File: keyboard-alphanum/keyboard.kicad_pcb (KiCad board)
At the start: 2 copper layers, 76.2 x 100.8 mm, 52 parts, among them J1 USB_B_Mini, U1 ATmega168PA-A, U2 CH340C, Y1 16MHz

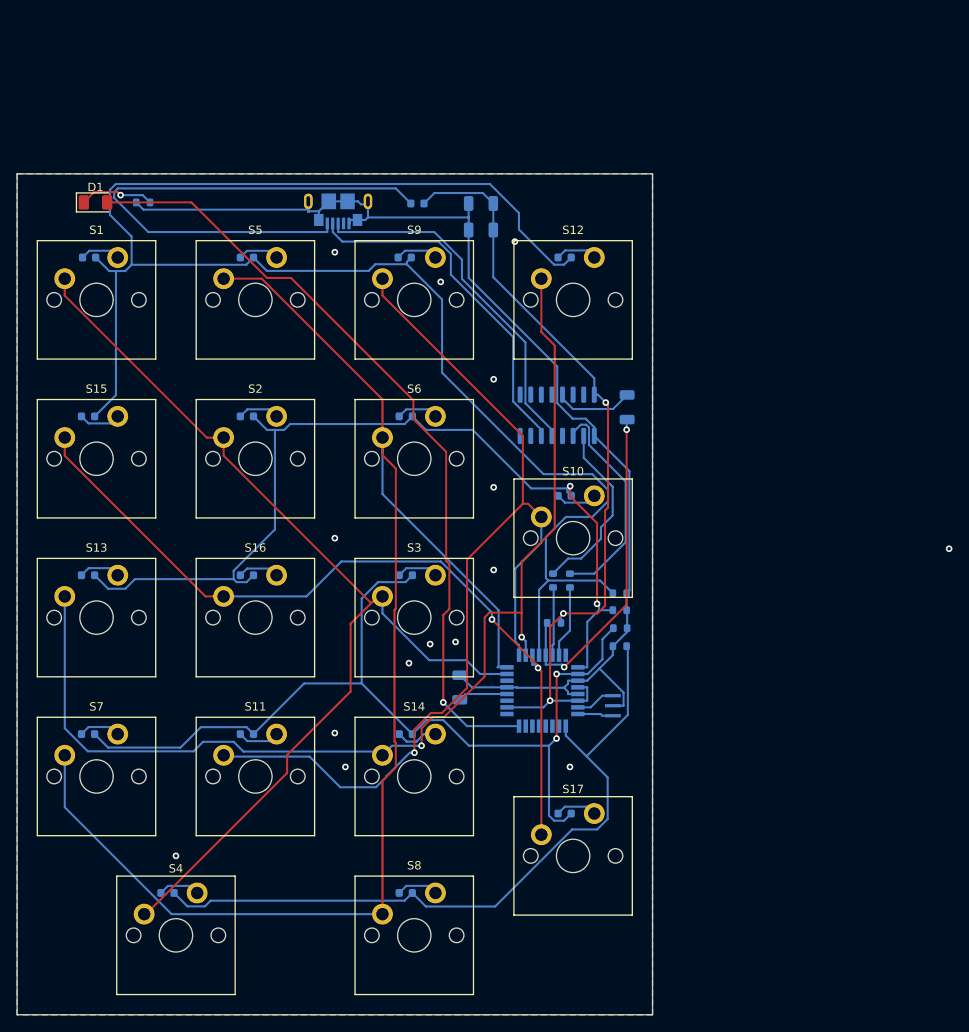
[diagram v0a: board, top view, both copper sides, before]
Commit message: Update keyboar pcb design
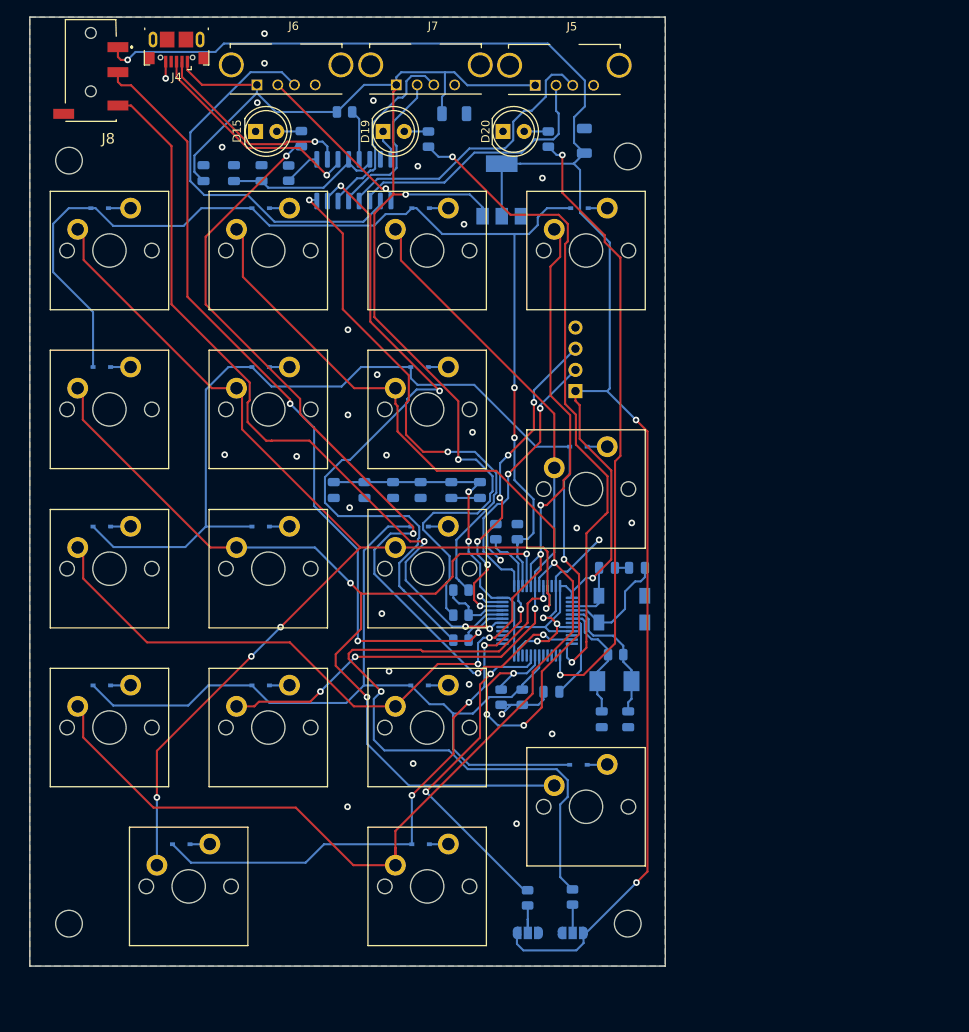
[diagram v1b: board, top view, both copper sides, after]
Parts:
- removed S1: NL, Switch_Keyboard_Cherry_MX:SW_Cherry_MX_PCB_1.00u
- removed S10: plus, Switch_Keyboard_Cherry_MX:SW_Cherry_MX_PCB_2.00u_90deg
- removed S11: 2, Switch_Keyboard_Cherry_MX:SW_Cherry_MX_PCB_1.00u
- removed S12: sub, Switch_Keyboard_Cherry_MX:SW_Cherry_MX_PCB_1.00u
- removed S13: 4, Switch_Keyboard_Cherry_MX:SW_Cherry_MX_PCB_1.00u
- removed S14: 3, Switch_Keyboard_Cherry_MX:SW_Cherry_MX_PCB_1.00u
- removed S15: 7, Switch_Keyboard_Cherry_MX:SW_Cherry_MX_PCB_1.00u
- removed S16: 5, Switch_Keyboard_Cherry_MX:SW_Cherry_MX_PCB_1.00u
- removed S17: enter, Switch_Keyboard_Cherry_MX:SW_Cherry_MX_PCB_2.00u_90deg
- removed S2: 8, Switch_Keyboard_Cherry_MX:SW_Cherry_MX_PCB_1.00u
- removed S3: 6, Switch_Keyboard_Cherry_MX:SW_Cherry_MX_PCB_1.00u
- removed S4: 0, Switch_Keyboard_Cherry_MX:SW_Cherry_MX_PCB_2.00u
- removed S5: div, Switch_Keyboard_Cherry_MX:SW_Cherry_MX_PCB_1.00u
- removed S6: 9, Switch_Keyboard_Cherry_MX:SW_Cherry_MX_PCB_1.00u
- removed S7: 1, Switch_Keyboard_Cherry_MX:SW_Cherry_MX_PCB_1.00u
- removed S8: point, Switch_Keyboard_Cherry_MX:SW_Cherry_MX_PCB_1.00u
- removed S9: mul, Switch_Keyboard_Cherry_MX:SW_Cherry_MX_PCB_1.00u
- added C10: 10nF, Capacitor_SMD:C_0805_2012Metric, B.Cu at (154.4, 91.0)
- added C11: 1uF, Capacitor_SMD:C_0805_2012Metric, B.Cu at (150.7, 91.0)
- added C12: 22uF, Capacitor_SMD:C_1206_3216Metric, B.Cu at (180.8, 49.1)
- added C13: 10uF, Capacitor_SMD:C_1206_3216Metric, B.Cu at (165.2, 45.9)
- added C14: 4.7uF, Capacitor_SMD:C_0805_2012Metric, B.Cu at (142.1, 53.0)
- added C15: 100nF, Capacitor_SMD:C_0805_2012Metric, B.Cu at (138.8, 53.0)
- added C16: 4.7uF, Capacitor_SMD:C_0805_2012Metric, B.Cu at (135.1, 53.0)
- added C5: 100nF, Capacitor_SMD:C_0805_2012Metric, B.Cu at (176.8, 115.2)
- added C6: 100nF, Capacitor_SMD:C_0805_2012Metric, B.Cu at (168.3, 91.0)
- added C7: 100nF, Capacitor_SMD:C_0805_2012Metric, B.Cu at (164.8, 91.0)
- added C8: 100nF, Capacitor_SMD:C_0805_2012Metric, B.Cu at (161.2, 91.0)
- added C9: 4.7uF, Capacitor_SMD:C_0805_2012Metric, B.Cu at (157.9, 91.0)
- added D20: ScrollLock, LED_THT:LED_D5.0mm, F.Cu at (171.0, 48.0)
- added H1: MountingHole_3.2mm_M3, MountingHole:MountingHole_3.2mm_M3, F.Cu at (119.0, 51.5)
- added H2: MountingHole_3.2mm_M3, MountingHole:MountingHole_3.2mm_M3, F.Cu at (186.0, 51.0)
- added H3: MountingHole_3.2mm_M3, MountingHole:MountingHole_3.2mm_M3, F.Cu at (119.0, 143.0)
- added H4: MountingHole_3.2mm_M3, MountingHole:MountingHole_3.2mm_M3, F.Cu at (186.0, 143.0)
- added J2: BOOT1, Jumper:SolderJumper-3_P1.3mm_Open_RoundedPad1.0x1.5mm, B.Cu at (174.0, 144.1)
- added J3: ST-Link, Connector_PinHeader_2.54mm:PinHeader_1x04_P2.54mm_Vertical, B.Cu at (179.7, 79.1)
- added J4: USB_B_Mini, common:USB_Micro-B_A01SB141B1-245, F.Cu at (131.9, 38.2)
- added J5: USB_A, common:USB_A_Molex_105057_Vertical, F.Cu at (174.9, 42.5)
- added J6: USB_A, common:USB_A_Molex_105057_Vertical, F.Cu at (141.5, 42.4)
- added J7: USB_A, common:USB_A_Molex_105057_Vertical, F.Cu at (158.2, 42.4)
- added J8: UART, common:PJ320D, F.Cu at (121.6, 40.7)
- added R10: 1K, Resistor_SMD:R_0805_2012Metric, B.Cu at (170.2, 96.0)
- added R11: 100K, Resistor_SMD:R_0805_2012Metric, B.Cu at (145.3, 53.0)
- added R12: 4.7K, Resistor_SMD:R_0805_2012Metric, B.Cu at (152.0, 45.7)
- added R13: 100K, Resistor_SMD:R_0805_2012Metric, B.Cu at (176.5, 48.9)
- added R14: 100K, Resistor_SMD:R_0805_2012Metric, B.Cu at (162.1, 48.9)
- added R15: 100K, Resistor_SMD:R_0805_2012Metric, B.Cu at (146.9, 48.9)
- added R9: 1K, Resistor_SMD:R_0805_2012Metric, B.Cu at (173.4, 115.8)
- added SW1: NL, Switch_Keyboard_Cherry_MX:SW_Cherry_MX_PCB_1.00u, F.Cu at (123.9, 62.3)
- added SW10: plus, Switch_Keyboard_Cherry_MX:SW_Cherry_MX_PCB_2.00u_90deg, F.Cu at (181.0, 90.9)
- added SW11: 2, Switch_Keyboard_Cherry_MX:SW_Cherry_MX_PCB_1.00u, F.Cu at (142.9, 119.5)
- added SW12: sub, Switch_Keyboard_Cherry_MX:SW_Cherry_MX_PCB_1.00u, F.Cu at (181.0, 62.3)
- added SW13: 4, Switch_Keyboard_Cherry_MX:SW_Cherry_MX_PCB_1.00u, F.Cu at (123.9, 100.4)
- added SW14: 3, Switch_Keyboard_Cherry_MX:SW_Cherry_MX_PCB_1.00u, F.Cu at (162.0, 119.5)
- added SW15: 7, Switch_Keyboard_Cherry_MX:SW_Cherry_MX_PCB_1.00u, F.Cu at (123.9, 81.3)
- added SW16: 5, Switch_Keyboard_Cherry_MX:SW_Cherry_MX_PCB_1.00u, F.Cu at (142.9, 100.4)
- added SW17: enter, Switch_Keyboard_Cherry_MX:SW_Cherry_MX_PCB_2.00u_90deg, F.Cu at (181.0, 129.0)
- added SW2: 8, Switch_Keyboard_Cherry_MX:SW_Cherry_MX_PCB_1.00u, F.Cu at (142.9, 81.3)
- added SW3: 6, Switch_Keyboard_Cherry_MX:SW_Cherry_MX_PCB_1.00u, F.Cu at (162.0, 100.4)
- added SW4: 0, Switch_Keyboard_Cherry_MX:SW_Cherry_MX_PCB_2.00u, F.Cu at (133.3, 138.5)
- added SW5: div, Switch_Keyboard_Cherry_MX:SW_Cherry_MX_PCB_1.00u, F.Cu at (142.9, 62.3)
- added SW6: 9, Switch_Keyboard_Cherry_MX:SW_Cherry_MX_PCB_1.00u, F.Cu at (162.0, 81.3)
- added SW7: 1, Switch_Keyboard_Cherry_MX:SW_Cherry_MX_PCB_1.00u, F.Cu at (123.9, 119.5)
- added SW8: dot, Switch_Keyboard_Cherry_MX:SW_Cherry_MX_PCB_1.00u, F.Cu at (162.0, 138.5)
- added SW9: mul, Switch_Keyboard_Cherry_MX:SW_Cherry_MX_PCB_1.00u, F.Cu at (162.0, 62.3)
- added U3: HS8836A, Package_SO:SOP-16_3.9x9.9mm_P1.27mm, B.Cu at (153.2, 53.8)
- added Y2: 32768MHz, Crystal:Crystal_SMD_SeikoEpson_MC306-4Pin_8.0x3.2mm, B.Cu at (185.3, 105.3)
- C1, C2, C4: value 0.1uF -> 22pF; footprint common:C_1206_3216Metric -> Capacitor_SMD:C_0805_2012Metric
- C3: value 10uF -> 22pF; footprint common:C_1206_3216Metric -> Capacitor_SMD:C_0805_2012Metric
- D1: value LED -> D_Small; footprint common:LED_1206_3216Metric -> Diode_SMD:D_SOD-323; moved to B.Cu
- D10, D11, D12, D13, D14, D16, D17, D18, D2, D3, D4, D5, D6, D7, D8, D9: value D -> D_Small; footprint common:D_0603_1608Metric -> Diode_SMD:D_SOD-323
- D15: value D -> NumLock; footprint common:D_0603_1608Metric -> LED_THT:LED_D5.0mm; moved to F.Cu
- D19: value D -> CapsLock; footprint common:D_0603_1608Metric -> LED_THT:LED_D5.0mm; moved to F.Cu
- J1: value USB_B_Mini -> BOOT0; footprint common:USB_Micro-B_GCT_USB3076-30-A -> Jumper:SolderJumper-3_P1.3mm_Open_RoundedPad1.0x1.5mm
- R1, R2: value 1K -> 100K; footprint common:R_0603_1608Metric -> Resistor_SMD:R_0805_2012Metric
- R3: value 1K -> 1M; footprint common:R_0603_1608Metric -> Resistor_SMD:R_0805_2012Metric
- R4: value 1K -> 4.7K; footprint common:R_0603_1608Metric -> Resistor_SMD:R_0805_2012Metric
- R5, R6: value 1K -> 20R; footprint common:R_0603_1608Metric -> Resistor_SMD:R_0805_2012Metric
- R7, R8: footprint common:R_0603_1608Metric -> Resistor_SMD:R_0805_2012Metric
- U1: value ATmega168PA-A -> STM32F103C6T6A; footprint Package_QFP:TQFP-32_7x7mm_P0.8mm -> Package_QFP:LQFP-48_7x7mm_P0.5mm
- U2: value CH340C -> LD1117S33TR; footprint Package_SO:SOIC-16_3.9x9.9mm_P1.27mm -> Package_TO_SOT_SMD:SOT-223-3_TabPin2
- Y1: value 16MHz -> 8MHz; footprint common:Resonator_SMD_Murata_CSTxExxV-3Pin_3.0x1.1mm -> Crystal:Crystal_SMD_Abracon_ABM3-2Pin_5.0x3.2mm
- moved R2 95.3 mm to (174.0, 139.9), turned to 90 degrees
- moved J1 91.0 mm to (179.4, 144.1), turned to 180 degrees
- moved D19 84.6 mm to (156.7, 48.0), turned to 0 degrees
- moved D5 82.9 mm to (142.0, 57.2), turned to 0 degrees
- moved D9 74.6 mm to (161.2, 57.2), turned to 0 degrees
- moved C2 64.3 mm to (186.1, 118.5), turned to 90 degrees
- moved D10 57.4 mm to (180.1, 85.8), turned to 0 degrees
- moved D16 57.2 mm to (122.9, 76.3), turned to 0 degrees
- moved D15 56.9 mm to (141.4, 48.0), turned to 0 degrees
- moved D14 54.2 mm to (161.0, 114.4), turned to 0 degrees
- moved D7 54.2 mm to (122.9, 114.4), turned to 0 degrees
- moved D11 54.1 mm to (142.0, 114.4), turned to 0 degrees
- moved D8 51.3 mm to (161.2, 133.5), turned to 0 degrees
- moved D18 45.8 mm to (180.1, 124.0), turned to 0 degrees
- moved C3 44.6 mm to (187.1, 100.3), turned to 0 degrees
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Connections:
- C1 pad 2: Net-(C1-Pad2) -> OSC_OUT
- C2 pad 1: +5V -> GND
- C2 pad 2: GND -> OSC_IN
- C3 pad 1: +5V -> GND
- C3 pad 2: GND -> OSC32_OUT
- C4 pad 1: Net-(C4-Pad1) -> GND
- C4 pad 2: RESET -> OSC32_IN
- D1 pad 1: Net-(D1-Pad1) -> I0
- D10 pad 1: I3 -> I1
- D11 pad 1: I0 -> I2
- D12 pad 1: I1 -> I0
- D13 pad 1: I2 -> I1
- D14 pad 1: I0 -> I2
- D15 pad 1: I1 -> GND
- D16 pad 1: I2 -> I0
- D17 pad 1: I0 -> I1
- D18 pad 1: I1 -> I2
- D19 pad 1: I2 -> GND
- D2 pad 1: I0 -> I1
- D3 pad 1: I1 -> I2
- D4 pad 1: I2 -> I3
- D5 pad 1: I3 -> I0
- D6 pad 1: +5V -> I1
- D7 pad 1: I0 -> I2
- D8 pad 1: I1 -> I3
- D9 pad 1: I2 -> I0
- J1 pad 1: Net-(D6-Pad2) -> +3.3V
- J1 pad 3: Net-(J1-Pad3) -> GND
- R1 pad 1: RESET -> Net-(J1-Pad2)
- R1 pad 2: +5V -> BOOT0
- R2 pad 1: Net-(D1-Pad1) -> Net-(J2-Pad2)
- R2 pad 2: GND -> BOOT1
- R3 pad 1: Net-(R3-Pad1) -> OSC_IN
- R3 pad 2: RX -> OSC_OUT
- R4 pad 1: Net-(R4-Pad1) -> K-DP
- R4 pad 2: TX -> VBUS
- R5 pad 1: I0 -> Net-(R5-Pad1)
- R5 pad 2: GND -> K-DP
- R6 pad 1: I1 -> Net-(R6-Pad1)
- R6 pad 2: GND -> K-DM
- R7 pad 1: I2 -> I0
- R8 pad 1: I3 -> I1
- U1 pad 1: I1 -> +3.3V
- U1 pad 11: unconnected-(U1-Pad11) -> NumLock
- U1 pad 12: unconnected-(U1-Pad12) -> CapsLock
- U1 pad 13: unconnected-(U1-Pad13) -> ScrLock
- U1 pad 16: Net-(D1-Pad2) -> unconnected-(U1-Pad16)
- U1 pad 18: +5V -> I2
- U1 pad 19: unconnected-(U1-Pad19) -> I1
- U1 pad 2: I2 -> unconnected-(U1-Pad2)
- U1 pad 20: Net-(C1-Pad2) -> BOOT1
- U1 pad 21: GND -> unconnected-(U1-Pad21)
- U1 pad 23: O0 -> GND
- U1 pad 24: O1 -> +3.3V
- U1 pad 25: O2 -> unconnected-(U1-Pad25)
- U1 pad 26: O3 -> unconnected-(U1-Pad26)
- U1 pad 27: O4 -> unconnected-(U1-Pad27)
- U1 pad 28: I0 -> unconnected-(U1-Pad28)
- U1 pad 29: RESET -> unconnected-(U1-Pad29)
- U1 pad 3: GND -> OSC32_IN
- U1 pad 30: RX -> TX
- U1 pad 31: TX -> RX
- U1 pad 32: unconnected-(U1-Pad32) -> K-DM
- U1 pad 4: +5V -> OSC32_OUT
- U1 pad 5: GND -> OSC_IN
- U1 pad 6: +5V -> OSC_OUT
- U1 pad 7: Net-(U1-Pad7) -> NRST
- U1 pad 8: Net-(U1-Pad8) -> GND
- U1 pad 9: I3 -> +3.3V
- U2 pad 2: Net-(R3-Pad1) -> +3.3V
- U2 pad 3: Net-(R4-Pad1) -> VBUS
- Y1 pad 1: Net-(U1-Pad8) -> OSC_IN
- Y1 pad 2: GND -> OSC_OUT
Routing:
- net +3.3V: track 0.00 -> 288.3 mm, vias 0 -> 6
- net VBUS: track 0.00 -> 160.5 mm, vias 0 -> 2
- net NumLock: track 0.00 -> 101.0 mm, vias 0 -> 4
- net +5V: track 94.1 -> 0.00 mm, vias 3 -> 0
- net Net-(D1-Pad2): track 95.1 -> 2.66 mm, vias 1 -> 0
- net RX: track 8.23 -> 99.5 mm, vias 0 -> 3
- net GND: track 141.7 -> 51.8 mm, vias 14 -> 33
- net TX: track 8.67 -> 92.8 mm, vias 0 -> 3
- net Net-(R6-Pad1): track 0.00 -> 83.4 mm, vias 0 -> 2
- net BOOT0: track 0.00 -> 80.8 mm, vias 0 -> 2
- net CapsLock: track 0.00 -> 80.2 mm, vias 0 -> 2
- net ScrLock: track 0.00 -> 74.3 mm, vias 0 -> 2
- net I0: track 204.5 -> 134.2 mm, vias 0 -> 2
- net Net-(R5-Pad1): track 0.00 -> 63.5 mm, vias 0 -> 2
- net Net-(D6-Pad2): track 65.5 -> 2.40 mm
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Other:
- board size 76.2 x 100.8 mm -> 76.2 x 113.8 mm

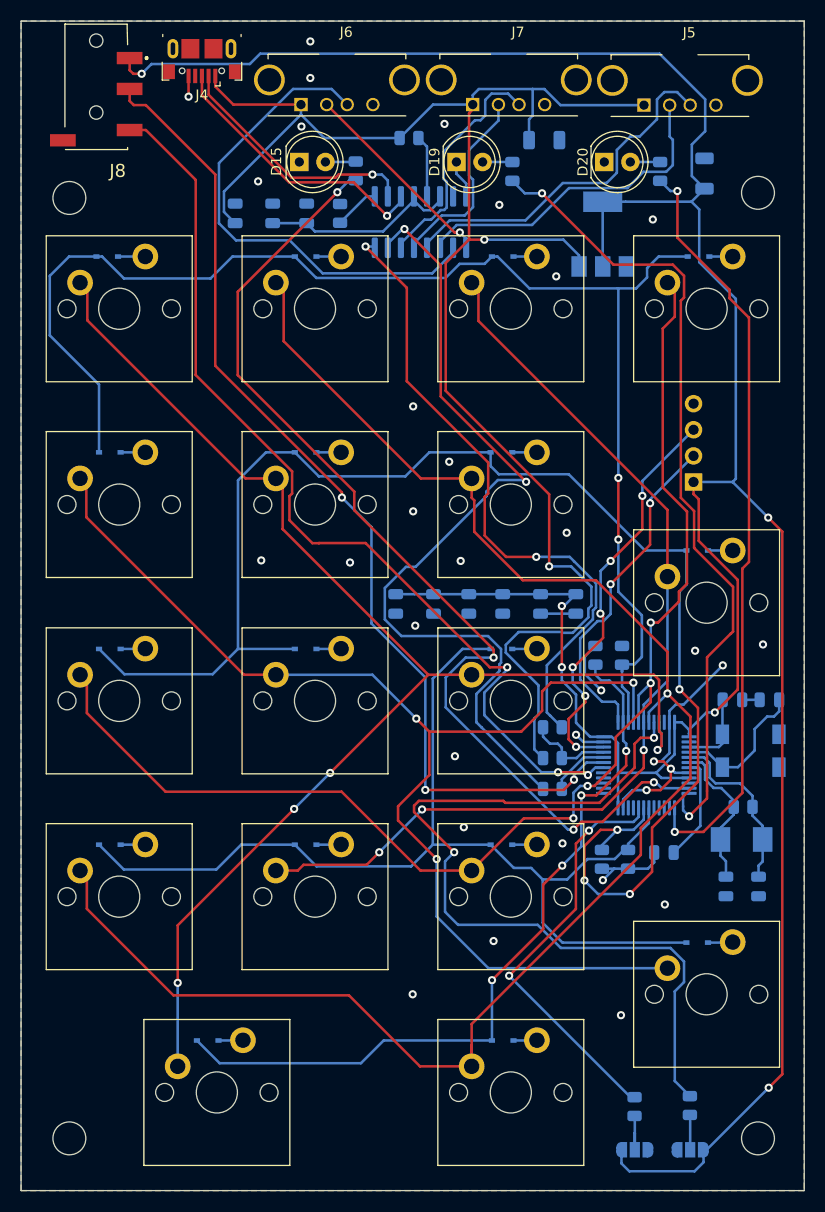
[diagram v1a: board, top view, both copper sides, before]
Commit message: Fix issues and update alphanum keyboard
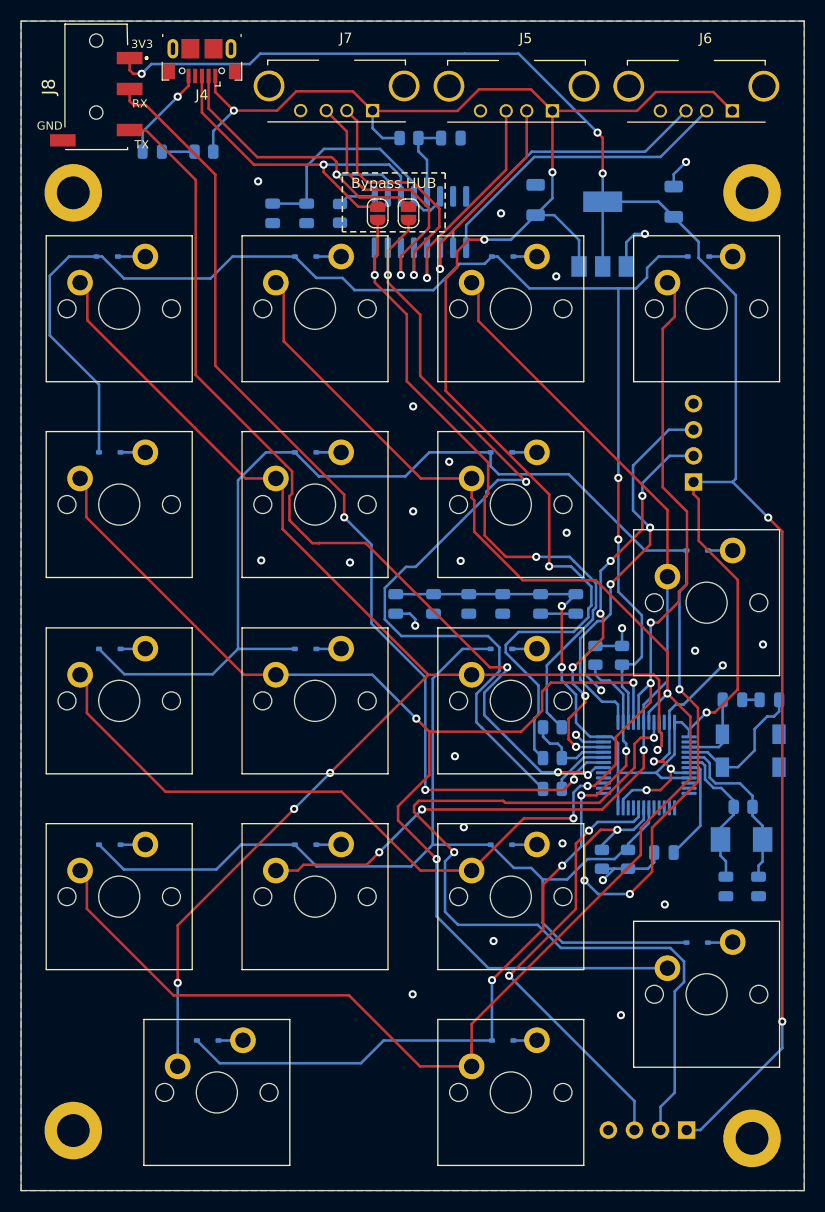
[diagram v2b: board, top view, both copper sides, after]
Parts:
- removed D19: CapsLock, LED_THT:LED_D5.0mm
- removed D20: ScrollLock, LED_THT:LED_D5.0mm
- removed J2: BOOT1, Jumper:SolderJumper-3_P1.3mm_Open_RoundedPad1.0x1.5mm
- removed R13, R14, R15, R2: 100K, Resistor_SMD:R_0805_2012Metric
- removed Y2: 32768MHz, Crystal:Crystal_SMD_SeikoEpson_MC306-4Pin_8.0x3.2mm
- added JP1: SolderJumper_2_Open, Jumper:SolderJumper-2_P1.3mm_Open_RoundedPad1.0x1.5mm, F.Cu at (149.0, 53.0)
- added JP2: SolderJumper_2_Open, Jumper:SolderJumper-2_P1.3mm_Open_RoundedPad1.0x1.5mm, F.Cu at (152.0, 53.0)
- added Y3: 32768MHz, Crystal:Crystal_SMD_SeikoEpson_MC306-4Pin_8.0x3.2mm, B.Cu at (185.3, 105.3)
- D15: value NumLock -> LED; footprint LED_THT:LED_D5.0mm -> LED_SMD:LED_0805_2012Metric; moved to B.Cu
- H1, H2, H3, H4: value MountingHole_3.2mm_M3 -> MountingHole; footprint MountingHole:MountingHole_3.2mm_M3 -> MountingHole:MountingHole_3.2mm_M3_DIN965_Pad
- J1: value BOOT0 -> Prog pings; footprint Jumper:SolderJumper-3_P1.3mm_Open_RoundedPad1.0x1.5mm -> Connector_PinHeader_2.54mm:PinHeader_1x04_P2.54mm_Vertical
- R1: value 100K -> 1K
- R12: value 4.7K -> 4R7
- moved H2 113.0 mm to (119.4, 142.2)
- moved R1 104.2 mm to (132.1, 47.0), turned to 0 degrees
- moved H4 92.0 mm to (185.4, 51.0)
- moved H3 66.4 mm to (185.4, 143.0)
- moved J6 35.0 mm to (176.5, 43.0)
- moved C16 22.2 mm to (156.1, 45.7), turned to 180 degrees
- moved J7 16.8 mm to (141.5, 43.0)
- moved J5 15.9 mm to (159.0, 43.0)
- moved D15 14.3 mm to (127.1, 47.0)
- moved C13 5.89 mm to (164.4, 51.7), turned to 90 degrees
- moved C12 4.06 mm to (177.8, 51.9)
- moved J1 1.95 mm to (179.1, 142.2), turned to 90 degrees
- moved H1 0.63 mm to (119.4, 51.0)
- turned C14 to -90 degrees
- turned C15 to -90 degrees
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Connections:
- net Net-(J4-Pad2) renamed DM
- net Net-(J4-Pad3) renamed DP
- C16 pad 2: VBUS -> Net-(U3-VCC)
- D15 pad 2: Net-(D15-Pad2) -> Net-(D15-A)
- J1 pad 2: Net-(J1-Pad2) -> BOOT0
- J1 pad 3: GND -> BOOT1
- J3 pad 2: SWCLK -> SWIO
- J3 pad 3: SWIO -> SWCLK
- R1 pad 1: Net-(J1-Pad2) -> Net-(D15-A)
- R1 pad 2: BOOT0 -> VBUS
- R12 pad 1: Net-(R12-Pad1) -> Net-(U3-VCC)
- U3 pad 13: Net-(R12-Pad1) -> Net-(U3-VCC)
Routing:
- net NumLock: track 101.0 -> 0.00 mm, vias 4 -> 0
- net CapsLock: track 80.2 -> 0.00 mm, vias 2 -> 0
- net ScrLock: track 74.3 -> 0.00 mm, vias 2 -> 0
- net +3.3V: track 288.3 -> 259.8 mm, vias 6 -> 8
- net Net-(J6-D+): track 48.1 -> 29.2 mm
- net GND: track 51.8 -> 69.8 mm, vias 33 -> 31
- net Net-(J5-D+): track 35.1 -> 22.4 mm, vias 0 -> 1
- net Net-(J5-D-): track 32.3 -> 20.9 mm, vias 0 -> 1
- net Net-(J6-D-): track 19.9 -> 30.2 mm, vias 1 -> 0
- net DM: track 24.5 -> 34.1 mm
- net Net-(U3-VCC): track 0.00 -> 8.23 mm
- net DP: track 27.6 -> 34.8 mm
- net Net-(J7-D-): track 19.0 -> 26.0 mm, vias 0 -> 1
- net Net-(R12-Pad1): track 6.03 -> 0.00 mm
- net V33: track 19.5 -> 24.9 mm
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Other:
- board text added: "3V3"
- board text added: "B0"
- board text added: "B1"
- board text added: "Bypass HUB"
- board text added: "GND"
- board text added: "Power LED for testing"
- board text added: "RX"
- board text added: "SWCLK"
- board text added: "SWIO"
- board text added: "TX"
